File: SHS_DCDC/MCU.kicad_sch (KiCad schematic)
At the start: 25 parts, among them J3 Conn_ARM_JTAG_SWD_10, J4 0022232041, J5 640456-2, SW1 TACT_SW, SW2 TACT_SW, SW3 TACT_SW, SW4 TACT_SW, U8 MIC5501-3.0YM5, Y1 2-SMD no lead

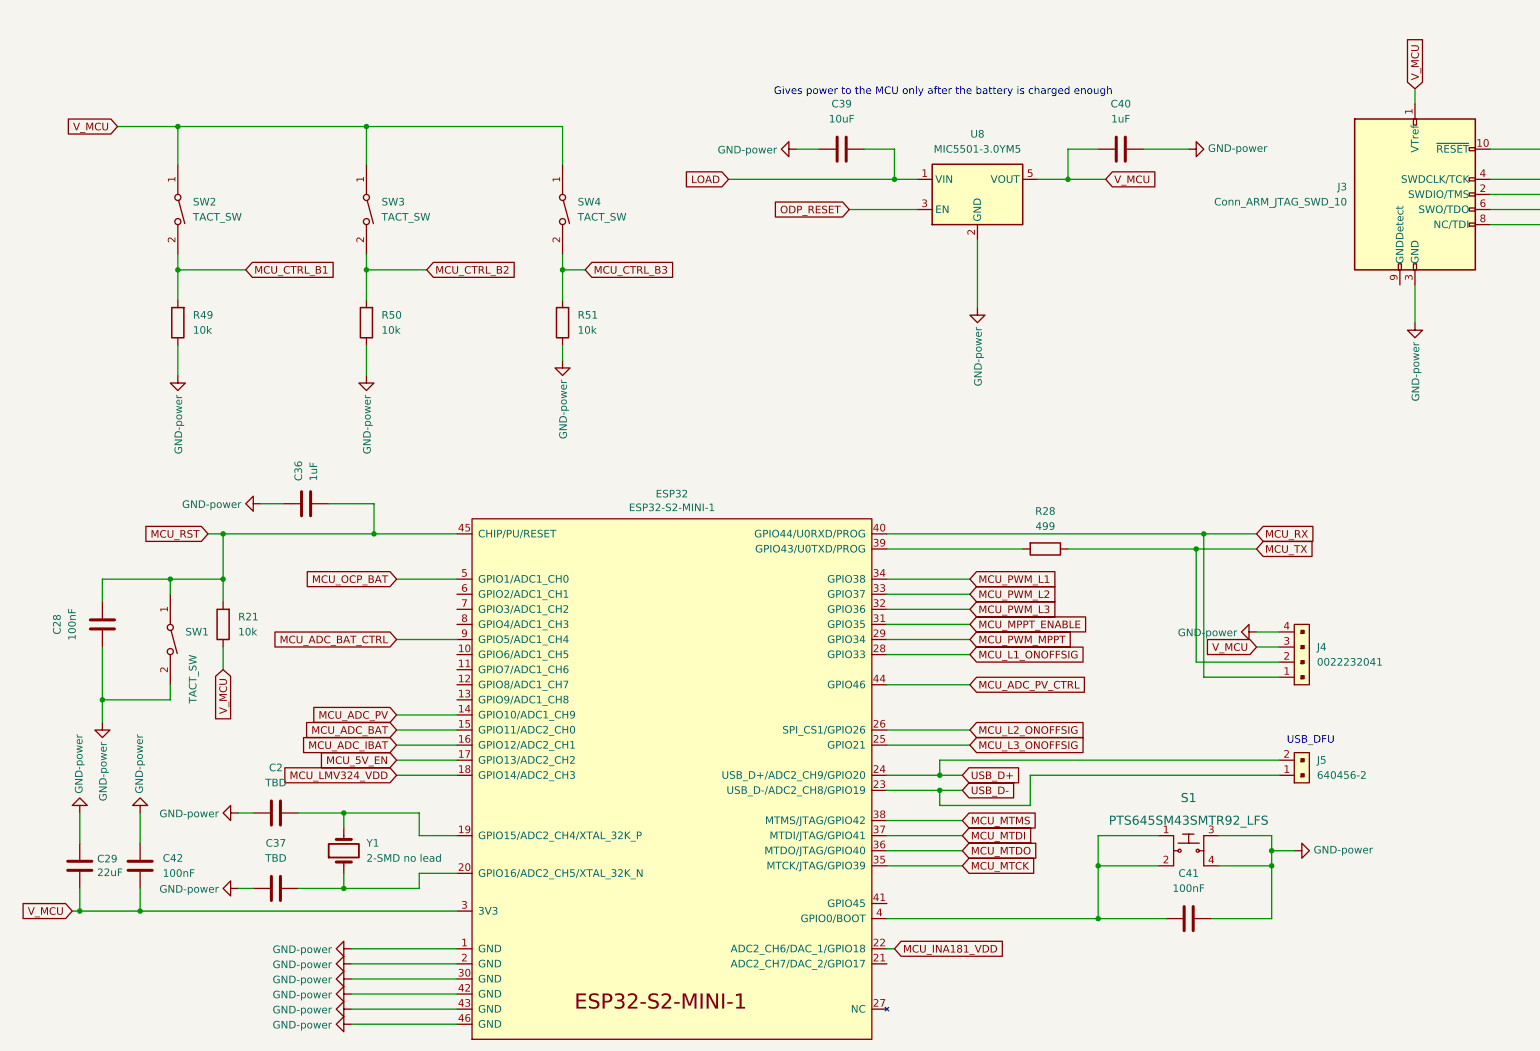
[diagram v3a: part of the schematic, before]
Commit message: PV input Power
Big modification on the PV input power protection, precisely on the reverse battery current protection, and also on the switch between direct PV charging and the DCDC converter
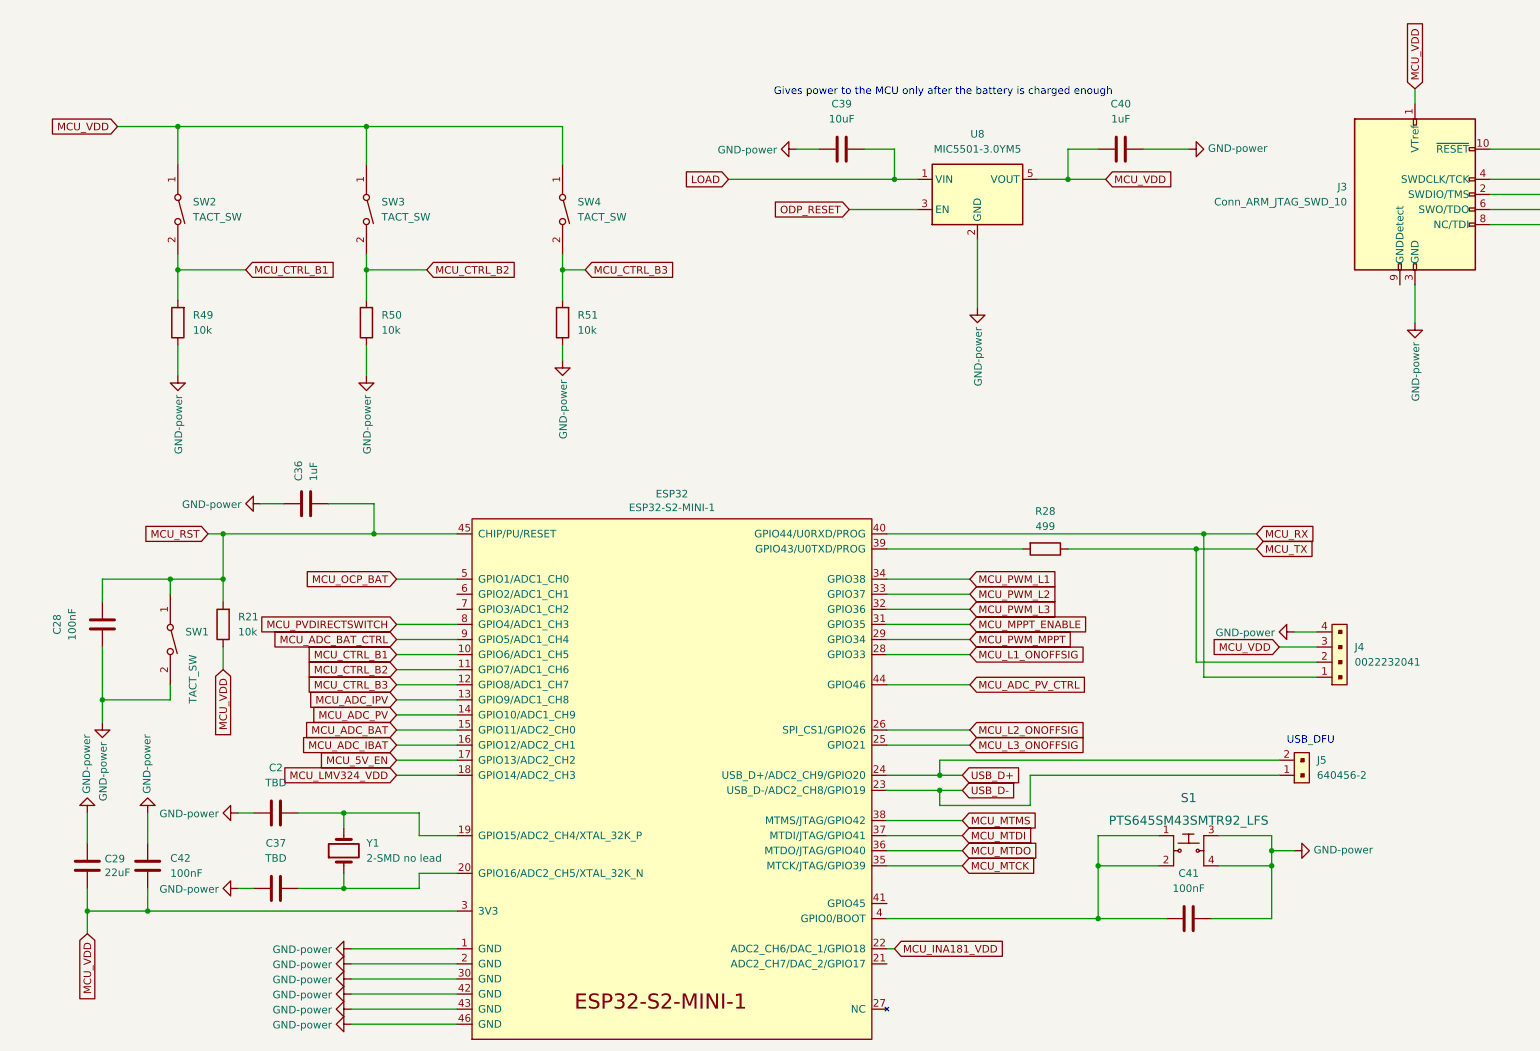
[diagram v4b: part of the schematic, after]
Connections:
- net MCU_CTRL_B1: now also ESP32.10 (GPIO6/ADC1_CH5)
- net MCU_CTRL_B2: now also ESP32.11 (GPIO7/ADC1_CH6)
- net MCU_CTRL_B3: now also ESP32.12 (GPIO8/ADC1_CH7)
- net MCU_ADC_IPV: now reaches ESP32.13 (GPIO9/ADC1_CH8)
- net MCU_PVDIRECTSWITCH: now reaches ESP32.8 (GPIO4/ADC1_CH3)
- net V_MCU renamed MCU_VDD
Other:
- moved on the sheet: C29, C42, J4

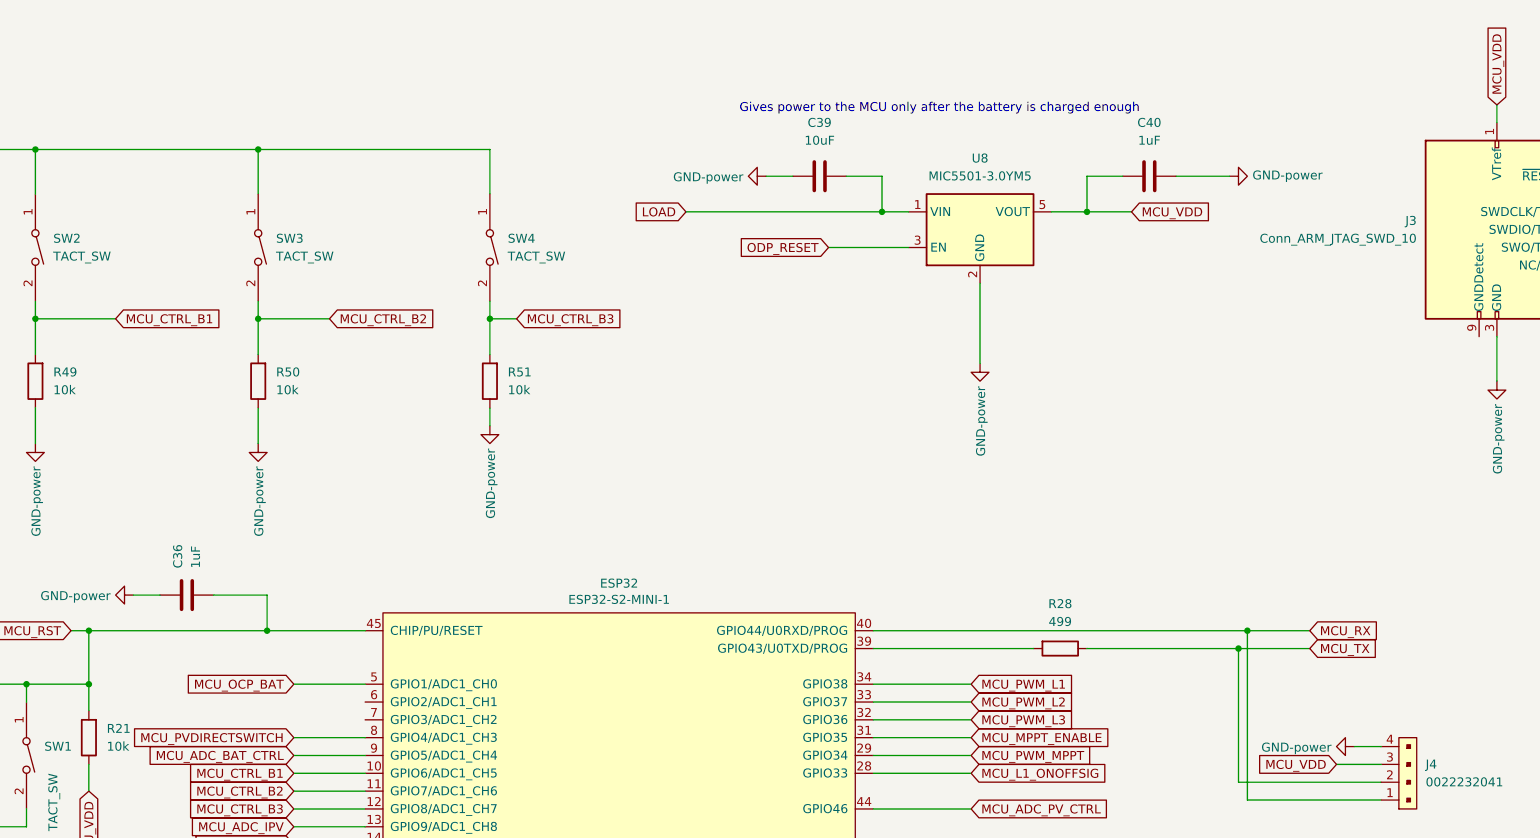
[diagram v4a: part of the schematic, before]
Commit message: Newbutton
New button whose job is to tell the MCU the user wants to establish a BLE connection with the SHS, in order to configure it.
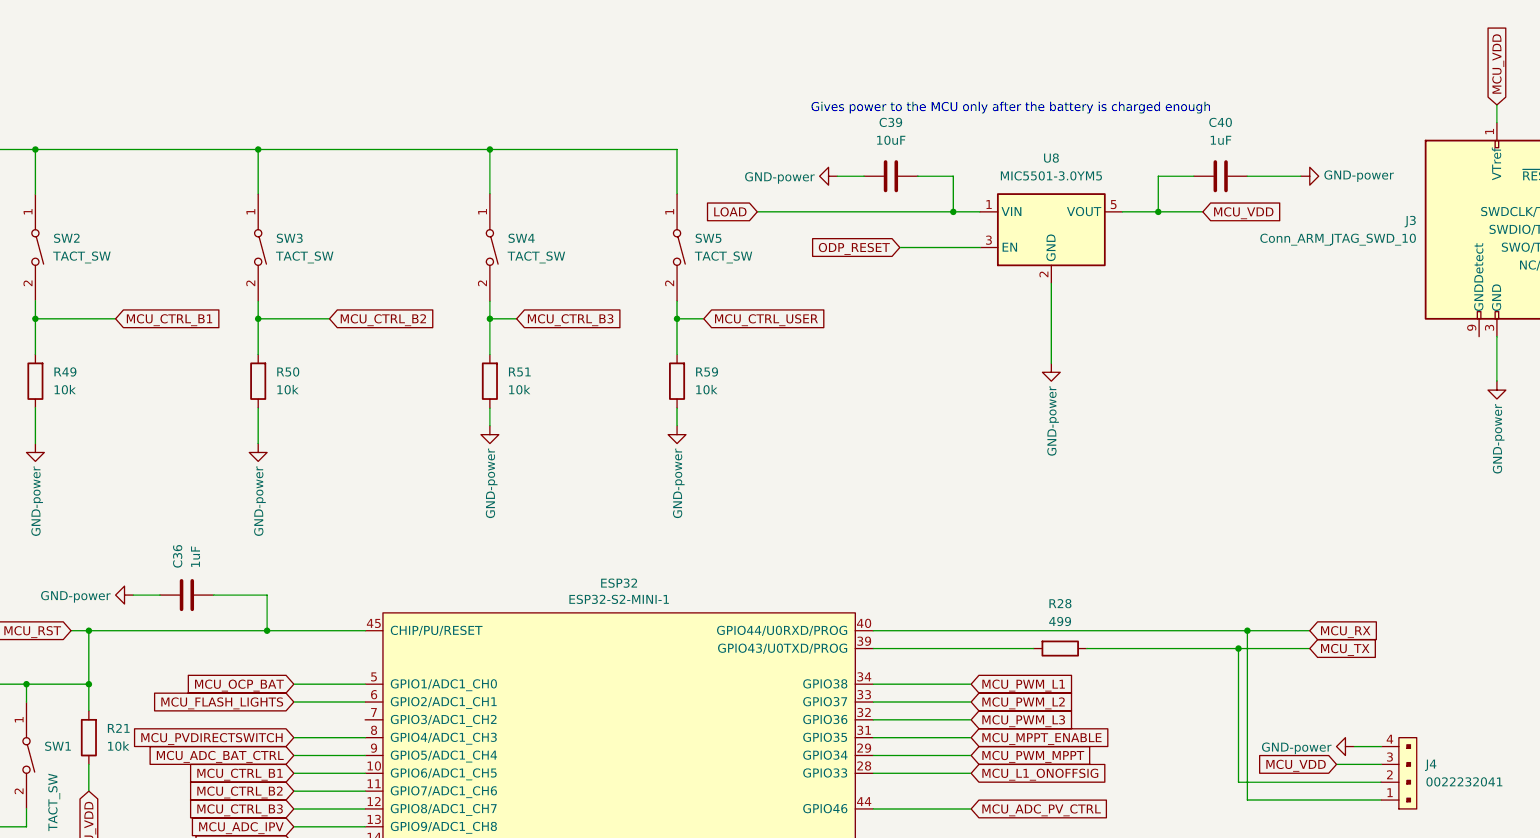
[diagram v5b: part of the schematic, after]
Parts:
- added R59: 10k, Resistor_SMD:R_0402_1005Metric, symbol Device:R
- added SW5: TACT_SW, SHS_DCDC:ESWITCH_TL1105, symbol SHS_DCDC:TACT_SW
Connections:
- net GND: now also R59.1
- net MCU_VDD: now also SW5.1
- net MCU_FLASH_LIGHTS: now reaches ESP32.6 (GPIO2/ADC1_CH1)
- new net MCU_CTRL_USER: R59.2, SW5.2
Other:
- moved on the sheet: C39, C40, U8

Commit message: LED
Placement of the 2nd dual LED
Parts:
- added BivarLEDguide1, BivarLEDguide2: MountingHole, SHS_DCDC:BIVAR VLP-XXX-F, symbol Mechanical:MountingHole
- added LED_BR1, LED_RG1: LED_Dual_AKKA, LED_SMD:LED_Kingbright_APHBM2012_2x1.25mm, symbol Device:LED_Dual_AKKA
- added R60, R61, R62, R63: 220, Resistor_SMD:R_0402_1005Metric, symbol Device:R
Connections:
- net GND: now also R60.1, R62.1
- net MCU_ADC_BAT_CTRL: now also ESP32.7 (GPIO3/ADC1_CH2); no longer ESP32.9 (GPIO5/ADC1_CH4)
- net MCU_ADC_IBAT: now also ESP32.9 (GPIO5/ADC1_CH4); no longer ESP32.16 (GPIO12/ADC2_CH1)
- net MCU_CTRL_B1: now also ESP32.6 (GPIO2/ADC1_CH1); no longer ESP32.10 (GPIO6/ADC1_CH5)
- net MCU_CTRL_B2: now also ESP32.28 (GPIO33); no longer ESP32.11 (GPIO7/ADC1_CH6)
- net MCU_CTRL_B3: now also ESP32.11 (GPIO7/ADC1_CH6); no longer ESP32.12 (GPIO8/ADC1_CH7)
- net MCU_FLASH_LIGHTS: now also ESP32.12 (GPIO8/ADC1_CH7); no longer ESP32.6 (GPIO2/ADC1_CH1)
- net MCU_L1_ONOFFSIG: now also ESP32.10 (GPIO6/ADC1_CH5); no longer ESP32.28 (GPIO33)
- net MCU_VDD: now also LED_BR1.4 (A2), LED_RG1.4 (A2)
- net MCU_LED_RG: now reaches ESP32.21 (ADC2_CH7/DAC_2/GPIO17)
- net MCU_LED_RG: now also LED_RG1.1 (A1), R61.2
- net MCU_BOOT0: now reaches C41.2, ESP32.4 (GPIO0/BOOT), S1.1, S1.2
- new net: LED_BR1.3 (K2), R63.1
- new net: LED_RG1.2 (K1), R60.2
- new net: LED_BR1.2 (K1), R62.2
- new net: LED_RG1.3 (K2), R61.1
- new net MCU_LED_BR: ESP32.16 (GPIO12/ADC2_CH1), LED_BR1.1 (A1), R63.2
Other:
- note added: "Gives power to the MCU only if the battery is charged enough"
- note removed: "Gives power to the MCU only after the battery is charged enough"
- moved on the sheet: C2, C28, C29, C36, C37, C39, C40, C41, C42, ESP32, J3, J4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

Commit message: Final_check stage
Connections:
- net MCU_CTRL_B3: now also ESP32.10 (GPIO6/ADC1_CH5); no longer ESP32.11 (GPIO7/ADC1_CH6)
- net MCU_L1_ONOFFSIG: now also ESP32.11 (GPIO7/ADC1_CH6); no longer ESP32.10 (GPIO6/ADC1_CH5)
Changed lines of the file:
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@@
     )
   )
-  (global_label "MCU_L1_ONOFFSIG" (shape input) (at 80.01 49.53 180) (fields_autoplaced)
+  (global_label "MCU_CTRL_B3" (shape input) (at 80.01 49.53 180) (fields_autoplaced)
     (effects (font (size 1.27 1.27)) (justify right))
-    (property "Intersheet References" "${INTERSHEET_REFS}" (id 0) (at 60.2082 49.6094 0)
+    (property "Intersheet References" "${INTERSHEET_REFS}" (id 0) (at 64.6834 49.4506 0)
       (effects (font (size 1.27 1.27)) (justify right) hide)
     )
@@
     )
   )
-  (global_label "MCU_CTRL_B3" (shape input) (at 80.01 52.07 180) (fields_autoplaced)
+  (global_label "MCU_L1_ONOFFSIG" (shape input) (at 80.01 52.07 180) (fields_autoplaced)
     (effects (font (size 1.27 1.27)) (justify right))
-    (property "Intersheet References" "${INTERSHEET_REFS}" (id 0) (at 64.6834 51.9906 0)
+    (property "Intersheet References" "${INTERSHEET_REFS}" (id 0) (at 60.2082 51.9906 0)
       (effects (font (size 1.27 1.27)) (justify right) hide)
     )

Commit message: Starting DRC
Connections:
- net MCU_ADC_PV_CTRL: now also ESP32.41 (GPIO45); no longer ESP32.44 (GPIO46)
- net MCU_CTRL_USER: now also ESP32.44 (GPIO46)
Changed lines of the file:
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@@
+    (stroke (width 0) (type default) (color 0 0 0 0))
+  )
+  (wire (pts (xy 162.56 91.44) (xy 175.26 91.44))
     (stroke (width 0) (type default) (color 0 0 0 0))
   )
@@
     )
   )
+  (global_label "MCU_ADC_PV_CTRL" (shape input) (at 175.26 91.44 0) (fields_autoplaced)
+    (effects (font (size 1.27 1.27)) (justify left))
+    (property "Intersheet References" "${INTERSHEET_REFS}" (id 0) (at 195.0618 91.3606 0)
+      (effects (font (size 1.27 1.27)) (justify left) hide)
+    )
+  )
   (global_label "MCU_L2_ONOFFSIG" (shape input) (at 176.53 62.23 0) (fields_autoplaced)
     (effects (font (size 1.27 1.27)) (justify left))
@@
     )
   )
-  (global_label "MCU_ADC_PV_CTRL" (shape input) (at 176.53 54.61 0) (fields_autoplaced)
-    (effects (font (size 1.27 1.27)) (justify left))
-    (property "Intersheet References" "${INTERSHEET_REFS}" (id 0) (at 196.3318 54.6894 0)
-      (effects (font (size 1.27 1.27)) (justify left) hide)
-    )
+  (global_label "MCU_CTRL_USER" (shape input) (at 176.53 54.61 0) (fields_autoplaced)
+    (effects (font (size 1.27 1.27)) (justify left))
+    (property "Intersheet References" "${INTERSHEET_REFS}" (id 0) (at 194.3361 54.5306 0)
+      (effects (font (size 1.27 1.27)) (justify left) hide)
+    )
